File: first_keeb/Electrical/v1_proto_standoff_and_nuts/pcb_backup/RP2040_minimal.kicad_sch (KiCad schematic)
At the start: 71 parts, among them J1 Conn_01x04_Socket, P1 USB-TYPE-C-016, Q1 BSS138, SW3 TS-1187A-B-A-B, SW5 TS-1187A-B-A-B, SW6 BUTT1, SW7 BUTT3, SW8 BUTT2, U1 ME6208A44M3G, U2 ME6206A25XG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

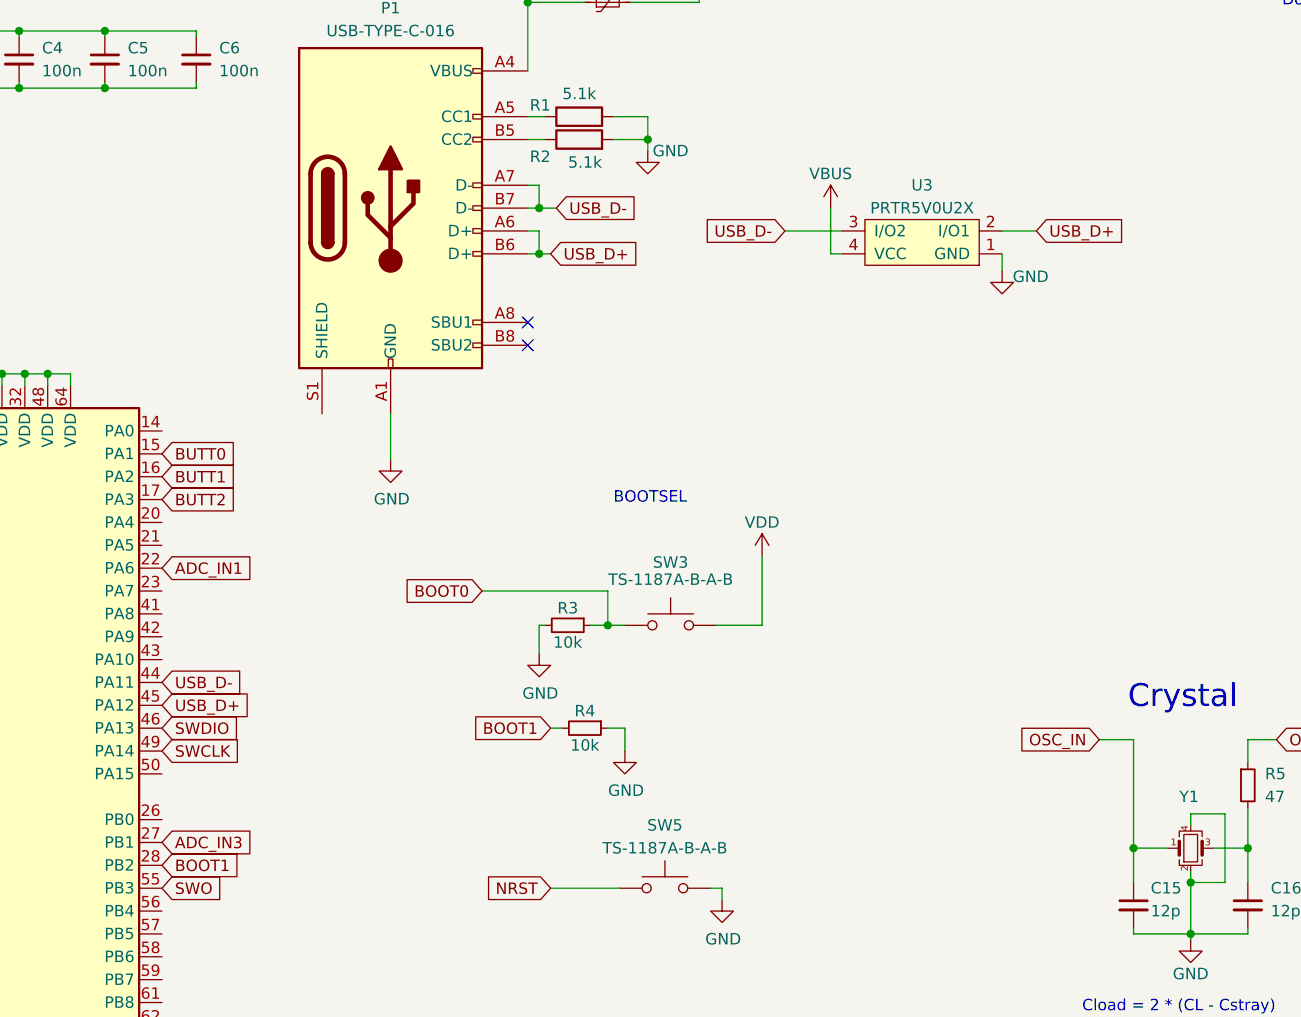
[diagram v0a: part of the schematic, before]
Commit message: stm fixes, still has different voltages
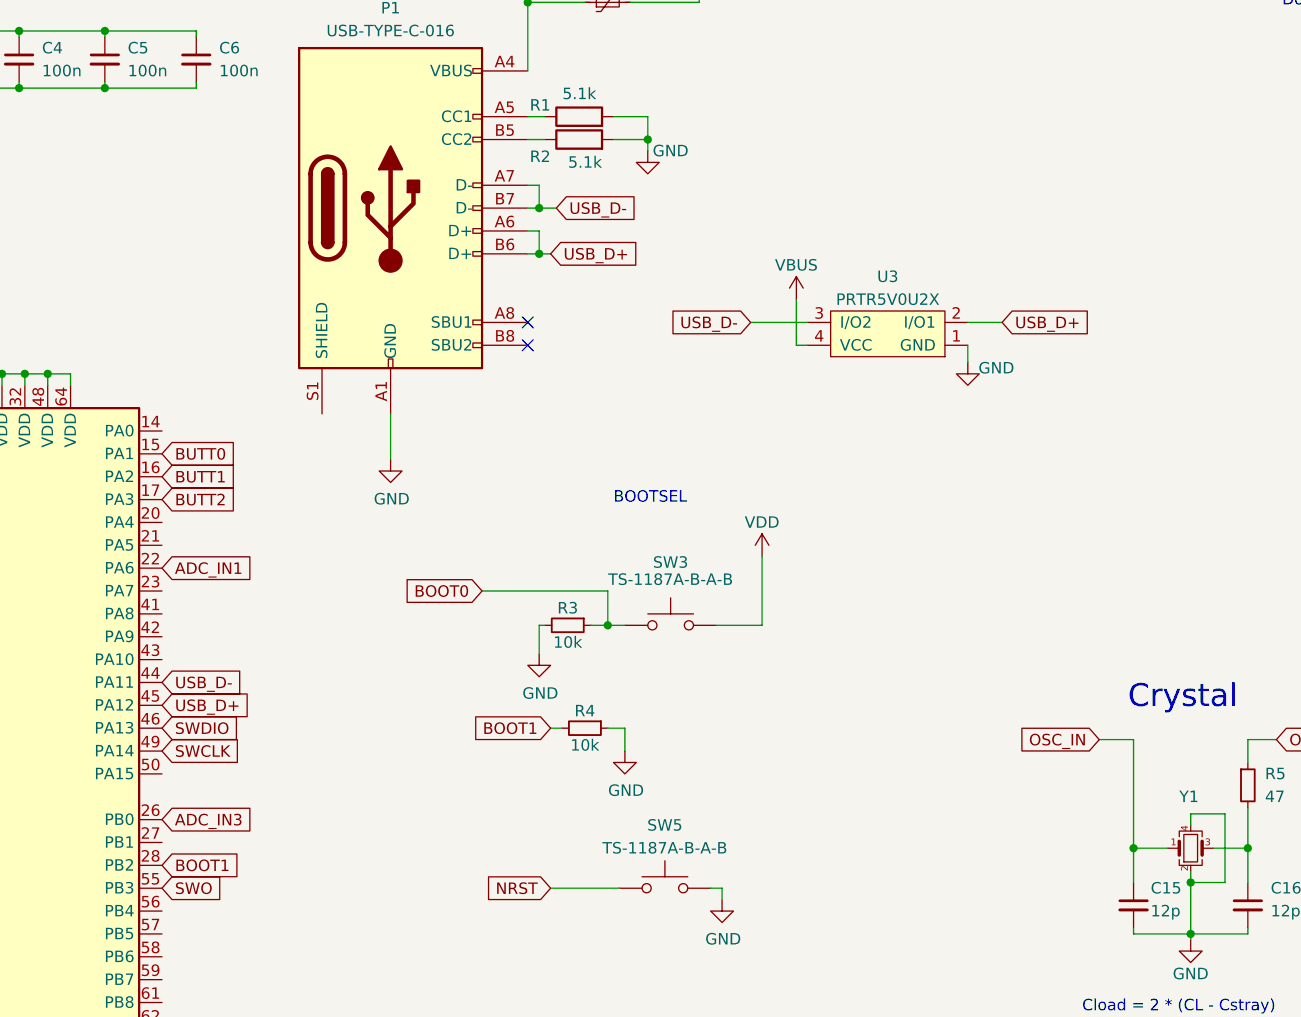
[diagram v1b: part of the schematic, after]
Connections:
- net ADC_IN3: now also U5.26 (PB0); no longer U5.27 (PB1)
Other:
- moved on the sheet: U3
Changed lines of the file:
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@@
     (stroke (width 0) (type default))
   )
-  (wire (pts (xy 183.515 59.055) (xy 182.245 59.055))
+  (wire (pts (xy 179.705 69.215) (xy 178.435 69.215))
     (stroke (width 0) (type default))
   )
@@
     (stroke (width 0) (type default))
   )
-  (wire (pts (xy 177.165 56.515) (xy 183.515 56.515))
+  (wire (pts (xy 173.355 66.675) (xy 179.705 66.675))
     (stroke (width 0) (type default))
   )
@@
     (stroke (width 0) (type default))
   )
-  (wire (pts (xy 201.295 56.515) (xy 205.105 56.515))
+  (wire (pts (xy 197.485 66.675) (xy 201.295 66.675))
     (stroke (width 0) (type default))
   )
@@
     (stroke (width 0) (type default))
   )
-  (wire (pts (xy 201.295 59.055) (xy 201.295 60.96))
+  (wire (pts (xy 197.485 69.215) (xy 197.485 71.12))
     (stroke (width 0) (type default))
   )
@@
     (stroke (width 0) (type default))
   )
-  (wire (pts (xy 182.245 59.055) (xy 182.245 53.975))
+  (wire (pts (xy 178.435 69.215) (xy 178.435 64.135))
     (stroke (width 0) (type default))
   )
@@
     )
   )
-  (global_label "ADC_IN3" (shape input) (at 107.95 124.46 0) (fields_autoplaced)
-    (effects (font (size 1.27 1.27)) (justify left))
-    (property "Intersheetrefs" "${INTERSHEET_REFS}" (at 117.9426 124.46 0)
-      (effects (font (size 1.27 1.27)) (justify left) hide)
-    )
-  )
   (global_label "USB_D+" (shape input) (at 151.13 59.055 0) (fields_autoplaced)
     (effects (font (size 1.27 1.27)) (justify left))
@@
     )
   )
-  (global_label "USB_D-" (shape input) (at 177.165 56.515 180) (fields_autoplaced)
+  (global_label "USB_D-" (shape input) (at 173.355 66.675 180) (fields_autoplaced)
     (effects (font (size 1.27 1.27)) (justify right))
-    (property "Intersheetrefs" "${INTERSHEET_REFS}" (at 167.2934 56.515 0)
+    (property "Intersheetrefs" "${INTERSHEET_REFS}" (at 163.4834 66.675 0)
       (effects (font (size 1.27 1.27)) (justify right) hide)
     )
@@
     )
   )
+  (global_label "ADC_IN3" (shape input) (at 107.95 121.92 0) (fields_autoplaced)
+    (effects (font (size 1.27 1.27)) (justify left))
+    (property "Intersheetrefs" "${INTERSHEET_REFS}" (at 117.9426 121.92 0)
+      (effects (font (size 1.27 1.27)) (justify left) hide)
+    )
+  )
   (global_label "BUTT1" (shape input) (at 54.61 243.205 180) (fields_autoplaced)
     (effects (font (size 1.27 1.27)) (justify right))
@@
     )
   )
-  (global_label "USB_D+" (shape input) (at 205.105 56.515 0) (fields_autoplaced)
+  (global_label "USB_D+" (shape input) (at 201.295 66.675 0) (fields_autoplaced)
     (effects (font (size 1.27 1.27)) (justify left))
-    (property "Intersheetrefs" "${INTERSHEET_REFS}" (at 214.9766 56.515 0)
+    (property "Intersheetrefs" "${INTERSHEET_REFS}" (at 211.1666 66.675 0)
       (effects (font (size 1.27 1.27)) (justify left) hide)
     )
@@
     )
   )
-  (symbol (lib_id "power:VBUS") (at 182.245 53.975 0) (unit 1)
+  (symbol (lib_id "power:VBUS") (at 178.435 64.135 0) (unit 1)
     (in_bom yes) (on_board yes) (dnp no)
-    (property "Reference" "#PWR015" (at 182.245 57.785 0)
+    (property "Reference" "#PWR015" (at 178.435 67.945 0)
       (effects (font (size 1.27 1.27)) hide)
     )
-    (property "Value" "VBUS" (at 182.245 50.165 0)
+    (property "Value" "VBUS" (at 178.435 60.325 0)
       (effects (font (size 1.27 1.27)))
     )
-    (property "Footprint" "" (at 182.245 53.975 0)
+    (property "Footprint" "" (at 178.435 64.135 0)
       (effects (font (size 1.27 1.27)) hide)
     )
-    (property "Datasheet" "" (at 182.245 53.975 0)
+    (property "Datasheet" "" (at 178.435 64.135 0)
       (effects (font (size 1.27 1.27)) hide)
     )
@@
     )
   )
-  (symbol (lib_id "keebio:PRTR5V0U2X") (at 192.405 57.785 180) (unit 1)
+  (symbol (lib_id "keebio:PRTR5V0U2X") (at 188.595 67.945 180) (unit 1)
     (in_bom yes) (on_board yes) (dnp no) (fields_autoplaced)
-    (property "Reference" "U3" (at 192.405 51.435 0)
+    (property "Reference" "U3" (at 188.595 61.595 0)
       (effects (font (size 1.27 1.27)))
     )
-    (property "Value" "PRTR5V0U2X" (at 192.405 53.975 0)
+    (property "Value" "PRTR5V0U2X" (at 188.595 64.135 0)
       (effects (font (size 1.27 1.27)))
     )
-    (property "Footprint" "Keebio-Parts:SOT-143B" (at 193.675 60.325 0)
+    (property "Footprint" "Keebio-Parts:SOT-143B" (at 189.865 70.485 0)
       (effects (font (size 1.27 1.27)) hide)
     )
-    (property "Datasheet" "" (at 193.675 60.325 0)
+    (property "Datasheet" "" (at 189.865 70.485 0)
       (effects (font (size 1.27 1.27)) hide)
     )
@@
     )
   )
-  (symbol (lib_id "power:GND") (at 201.295 60.96 0) (unit 1)
+  (symbol (lib_id "power:GND") (at 197.485 71.12 0) (unit 1)
     (in_bom yes) (on_board yes) (dnp no)
-    (property "Reference" "#PWR017" (at 201.295 67.31 0)
+    (property "Reference" "#PWR017" (at 197.485 77.47 0)
       (effects (font (size 1.27 1.27)) hide)
     )
-    (property "Value" "GND" (at 204.47 61.595 0)
+    (property "Value" "GND" (at 200.66 71.755 0)
       (effects (font (size 1.27 1.27)))
     )
-    (property "Footprint" "" (at 201.295 60.96 0)
+    (property "Footprint" "" (at 197.485 71.12 0)
       (effects (font (size 1.27 1.27)) hide)
     )
-    (property "Datasheet" "" (at 201.295 60.96 0)
+    (property "Datasheet" "" (at 197.485 71.12 0)
       (effects (font (size 1.27 1.27)) hide)
     )
